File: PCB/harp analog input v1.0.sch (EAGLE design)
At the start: 109 parts, among them IC1 USBLC6-2SC6, IC10 SN74LVC1G125, IC11 SN74LVC1G125, IC12 SN74LVC1G125, IC13 AD7606-4, IC14 M74VHC1GT50DTT1G, IC15 M74VHC1GT50DTT1G, IC2 DC-DC-SIP-5, IC3 FT232RL, IC4 TPS78630DCQ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

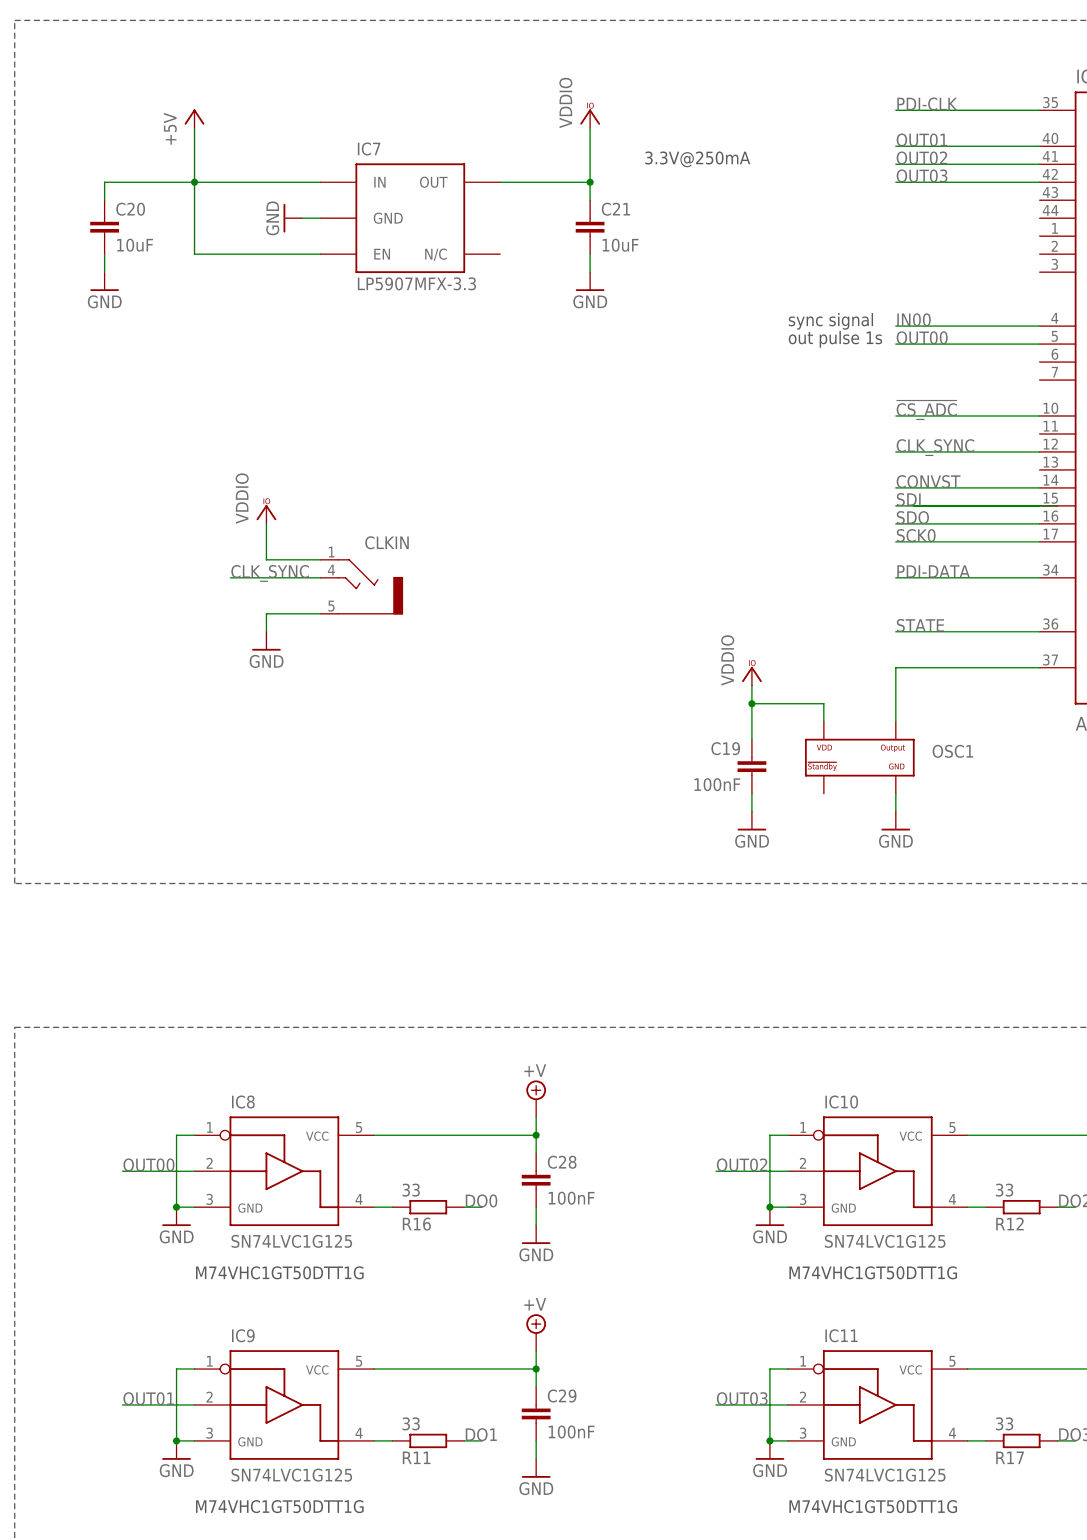
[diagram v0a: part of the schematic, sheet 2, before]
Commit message: Re-organized DO alignment from left (DO0) to right (DO3)
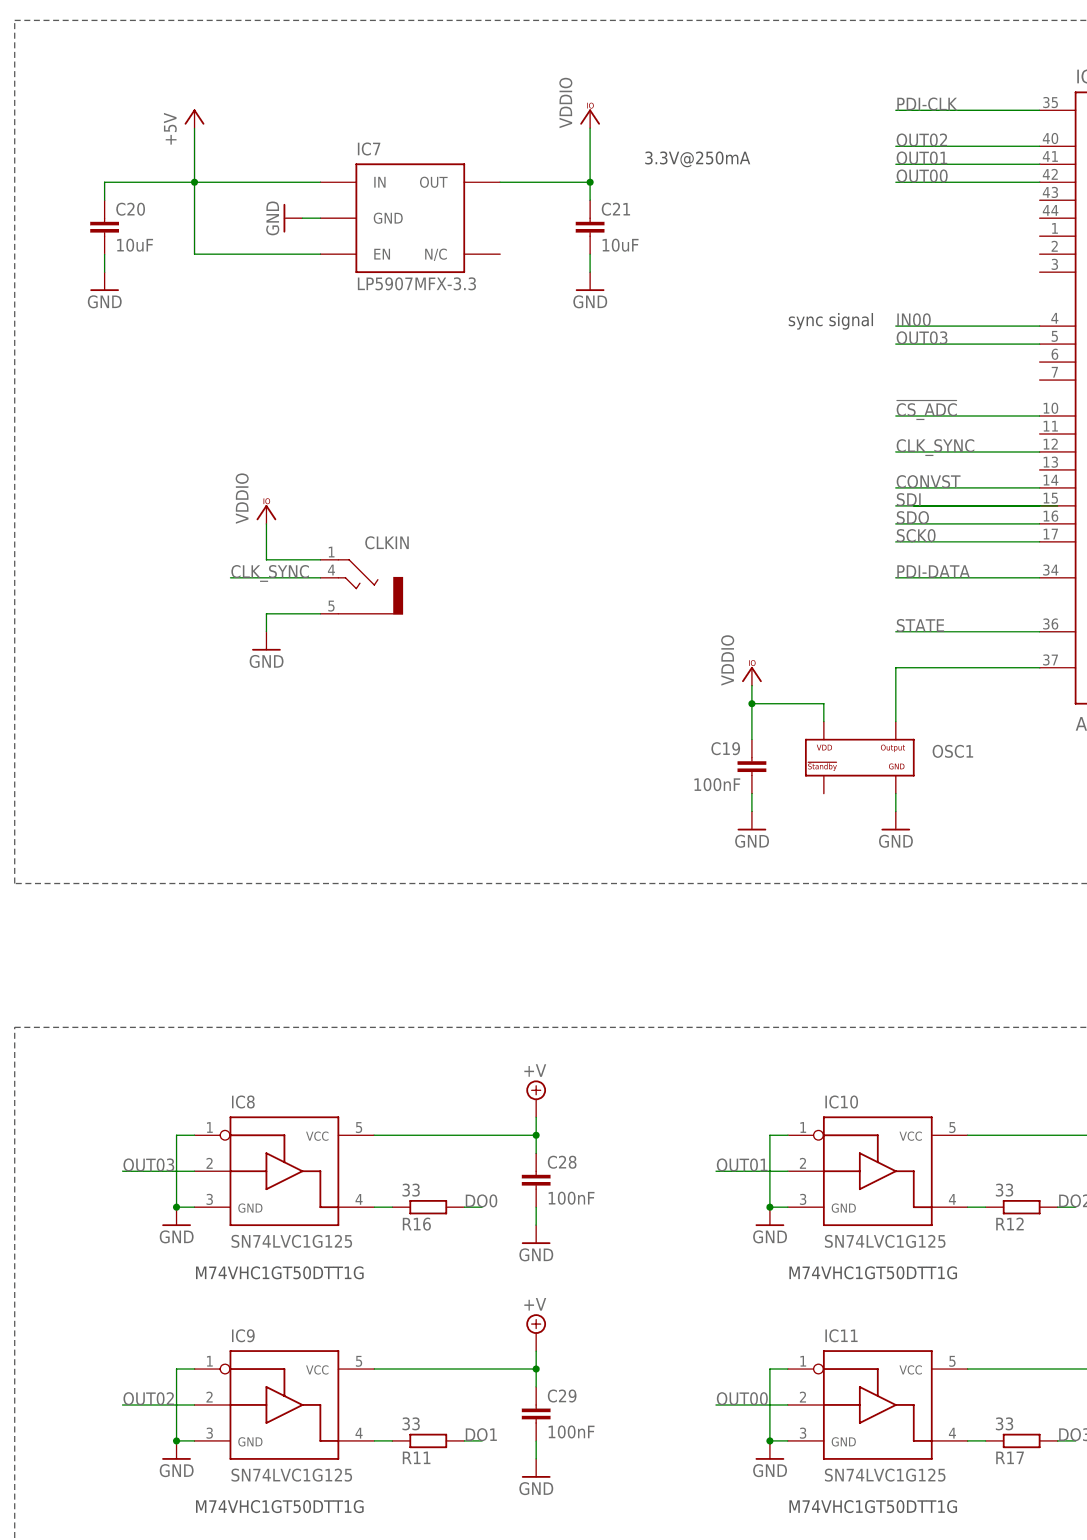
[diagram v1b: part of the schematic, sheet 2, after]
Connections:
- net OUT00: now also IC11.P$2, IC6.PA2/ADC2; no longer IC6.PB1/ADC9, IC8.P$2
- net OUT01: now also IC10.P$2, IC6.PA1/ADC1; no longer IC6.PA0/ADC0/AREF, IC9.P$2
- net OUT02: now also IC6.PA0/ADC0/AREF, IC9.P$2; no longer IC10.P$2, IC6.PA1/ADC1
- net OUT03: now also IC6.PB1/ADC9, IC8.P$2; no longer IC11.P$2, IC6.PA2/ADC2
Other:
- note removed: "out pulse 1s"
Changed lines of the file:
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@@
 <?xml version="1.0" encoding="utf-8"?>
 <!DOCTYPE eagle SYSTEM "eagle.dtd">
-<eagle version="9.6.2">
+<eagle version="9.5.1">
 <drawing>
 <settings>
@@
 <text x="109.22" y="226.06" size="1.778" layer="97">3.3V@250mA</text>
 <text x="129.54" y="203.2" size="1.778" layer="97">sync signal</text>
-<text x="129.54" y="200.66" size="1.778" layer="97">out pulse 1s</text>
 <text x="292.1" y="10.16" size="1.778" layer="94" ratio="10">Licensed under the TAPR Open
 Hardware License (www.tapr.org/OHL)
@@
 </segment>
 </net>
-<net name="OUT00" class="0">
+<net name="OUT03" class="0">
 <segment>
 <wire x1="165.1" y1="200.66" x2="144.78" y2="200.66" width="0.1524" layer="91"/>
@@
 </segment>
 </net>
-<net name="OUT03" class="0">
+<net name="OUT00" class="0">
 <segment>
 <wire x1="165.1" y1="223.52" x2="144.78" y2="223.52" width="0.1524" layer="91"/>
@@
 </segment>
 </net>
-<net name="OUT01" class="0">
+<net name="OUT02" class="0">
 <segment>
 <wire x1="165.1" y1="228.6" x2="144.78" y2="228.6" width="0.1524" layer="91"/>
@@
 </segment>
 </net>
-<net name="OUT02" class="0">
+<net name="OUT01" class="0">
 <segment>
 <wire x1="165.1" y1="226.06" x2="144.78" y2="226.06" width="0.1524" layer="91"/>

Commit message: Correct minor DRC and net labelling from merge
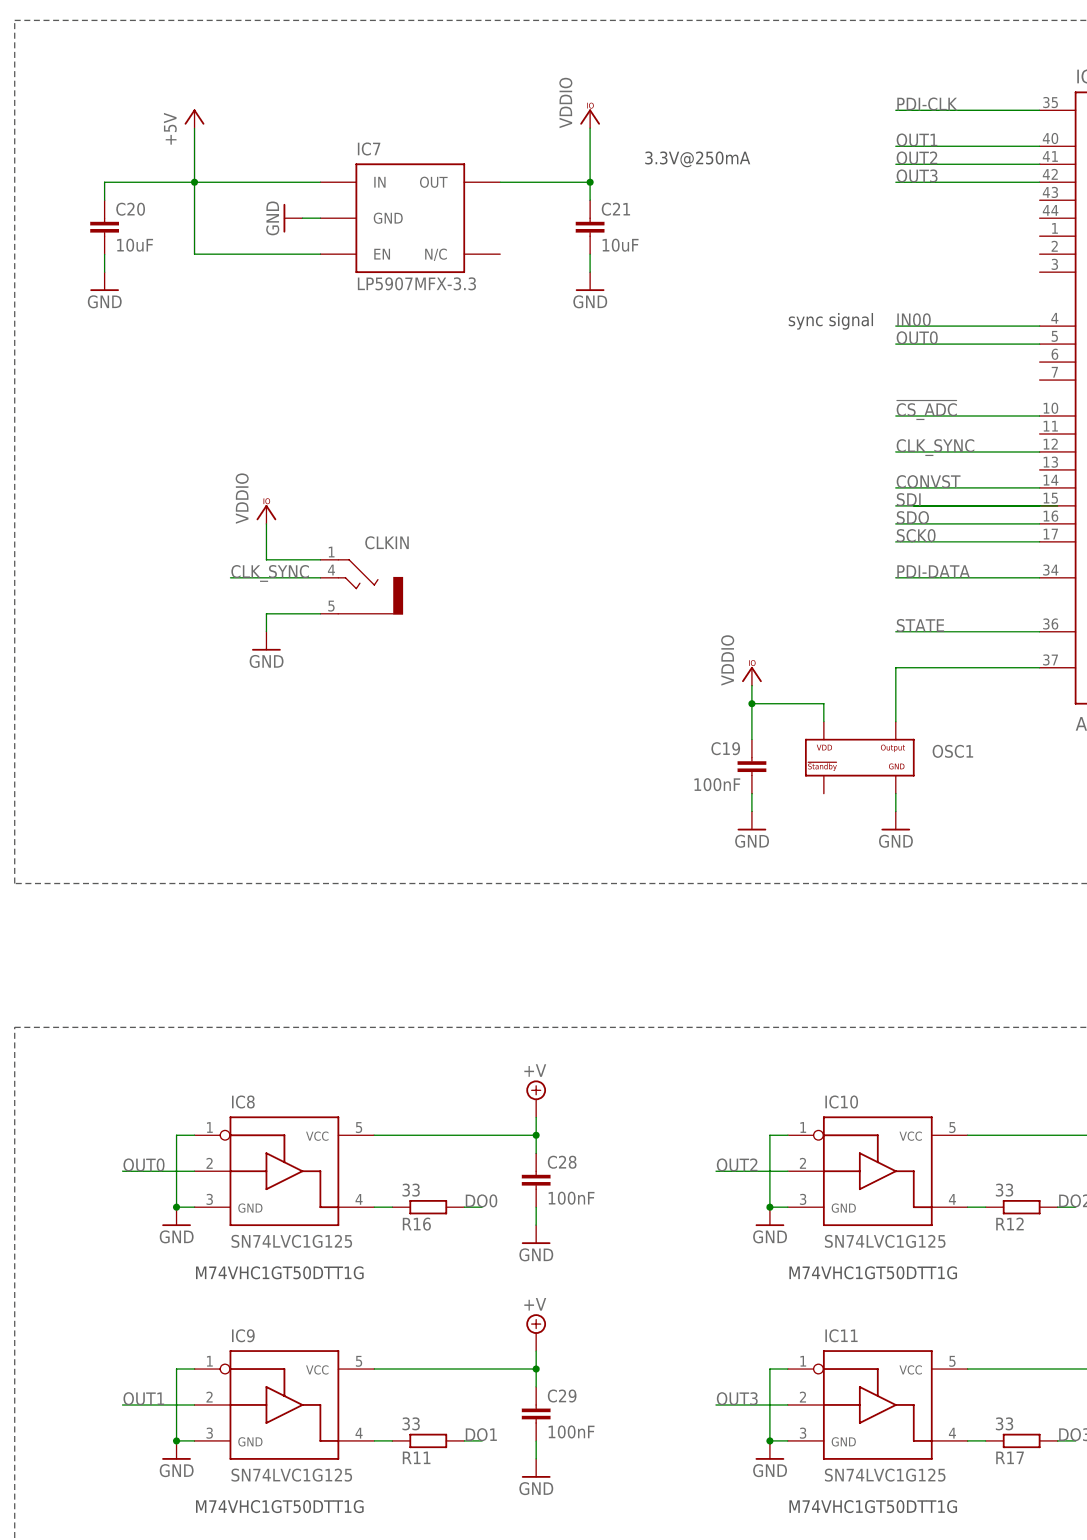
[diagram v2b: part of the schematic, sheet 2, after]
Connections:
- net OUT00 renamed OUT3
- net OUT01 renamed OUT2
- net OUT02 renamed OUT1
- net OUT03 renamed OUT0
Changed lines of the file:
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@@
 <?xml version="1.0" encoding="utf-8"?>
 <!DOCTYPE eagle SYSTEM "eagle.dtd">
-<eagle version="9.5.1">
+<eagle version="9.6.2">
 <drawing>
 <settings>
@@
 </segment>
 </net>
-<net name="OUT03" class="0">
+<net name="OUT0" class="0">
 <segment>
 <wire x1="165.1" y1="200.66" x2="144.78" y2="200.66" width="0.1524" layer="91"/>
@@
 </segment>
 </net>
-<net name="OUT00" class="0">
+<net name="OUT3" class="0">
 <segment>
 <wire x1="165.1" y1="223.52" x2="144.78" y2="223.52" width="0.1524" layer="91"/>
@@
 </segment>
 </net>
-<net name="OUT02" class="0">
+<net name="OUT1" class="0">
 <segment>
 <wire x1="165.1" y1="228.6" x2="144.78" y2="228.6" width="0.1524" layer="91"/>
@@
 </segment>
 </net>
-<net name="OUT01" class="0">
+<net name="OUT2" class="0">
 <segment>
 <wire x1="165.1" y1="226.06" x2="144.78" y2="226.06" width="0.1524" layer="91"/>

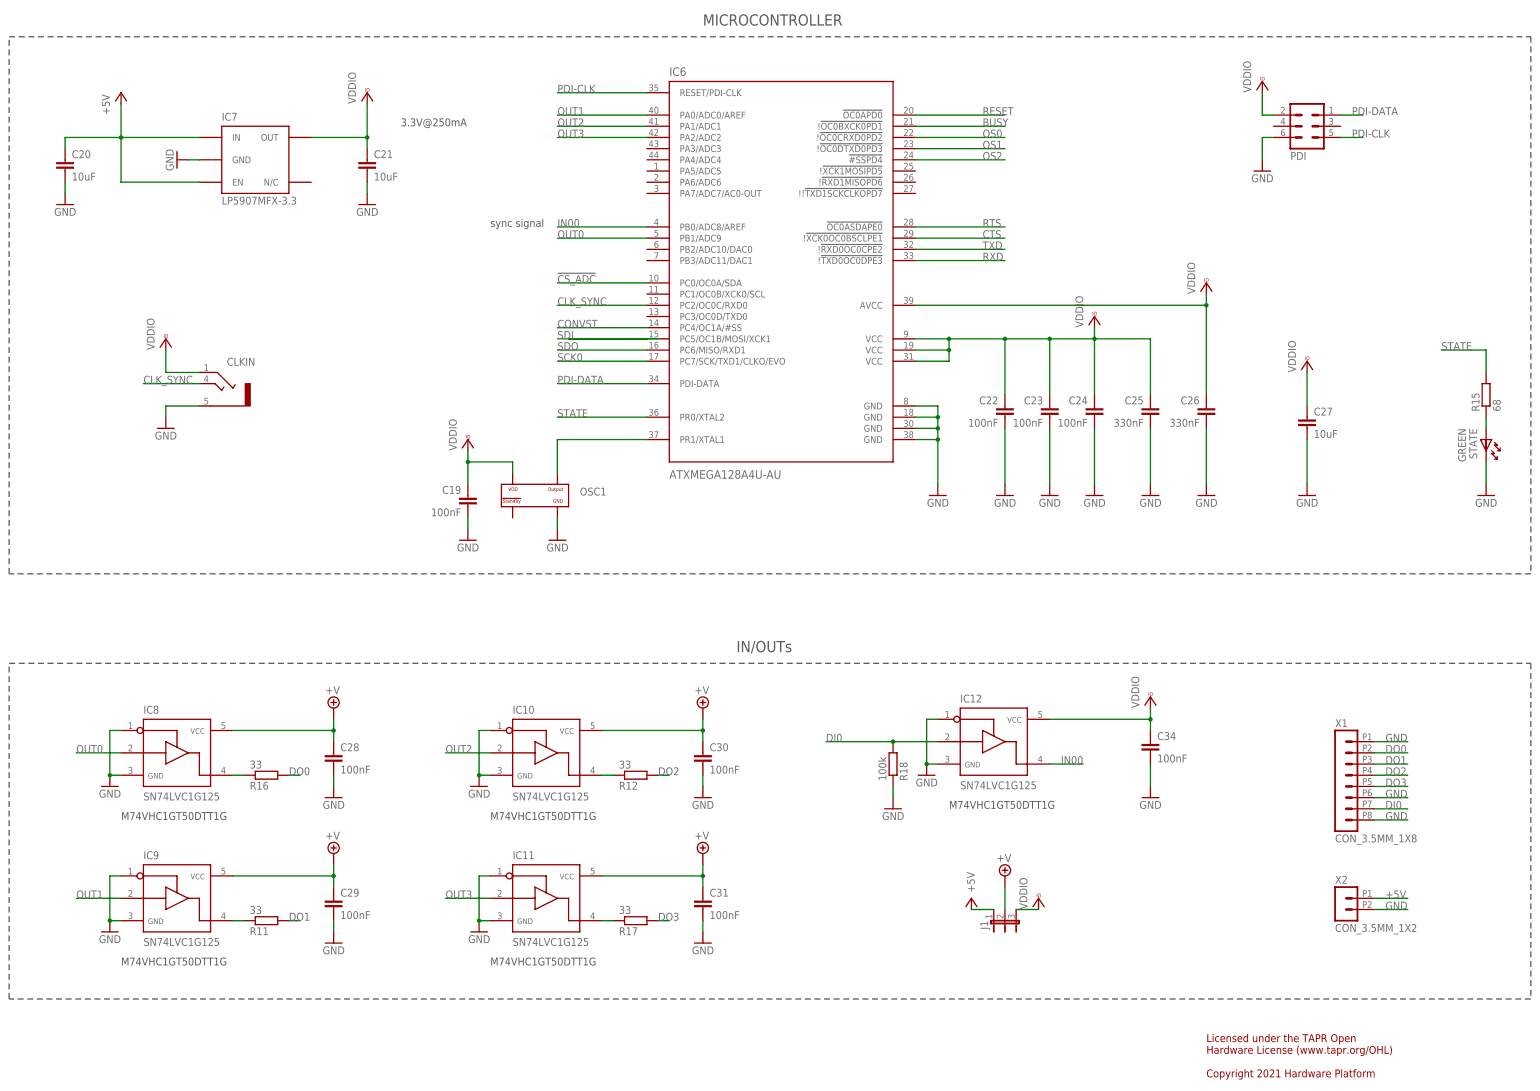
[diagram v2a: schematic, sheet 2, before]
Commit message: Add CONVST pin/swap CS_ADC
To allow for future higher speed acquisitions
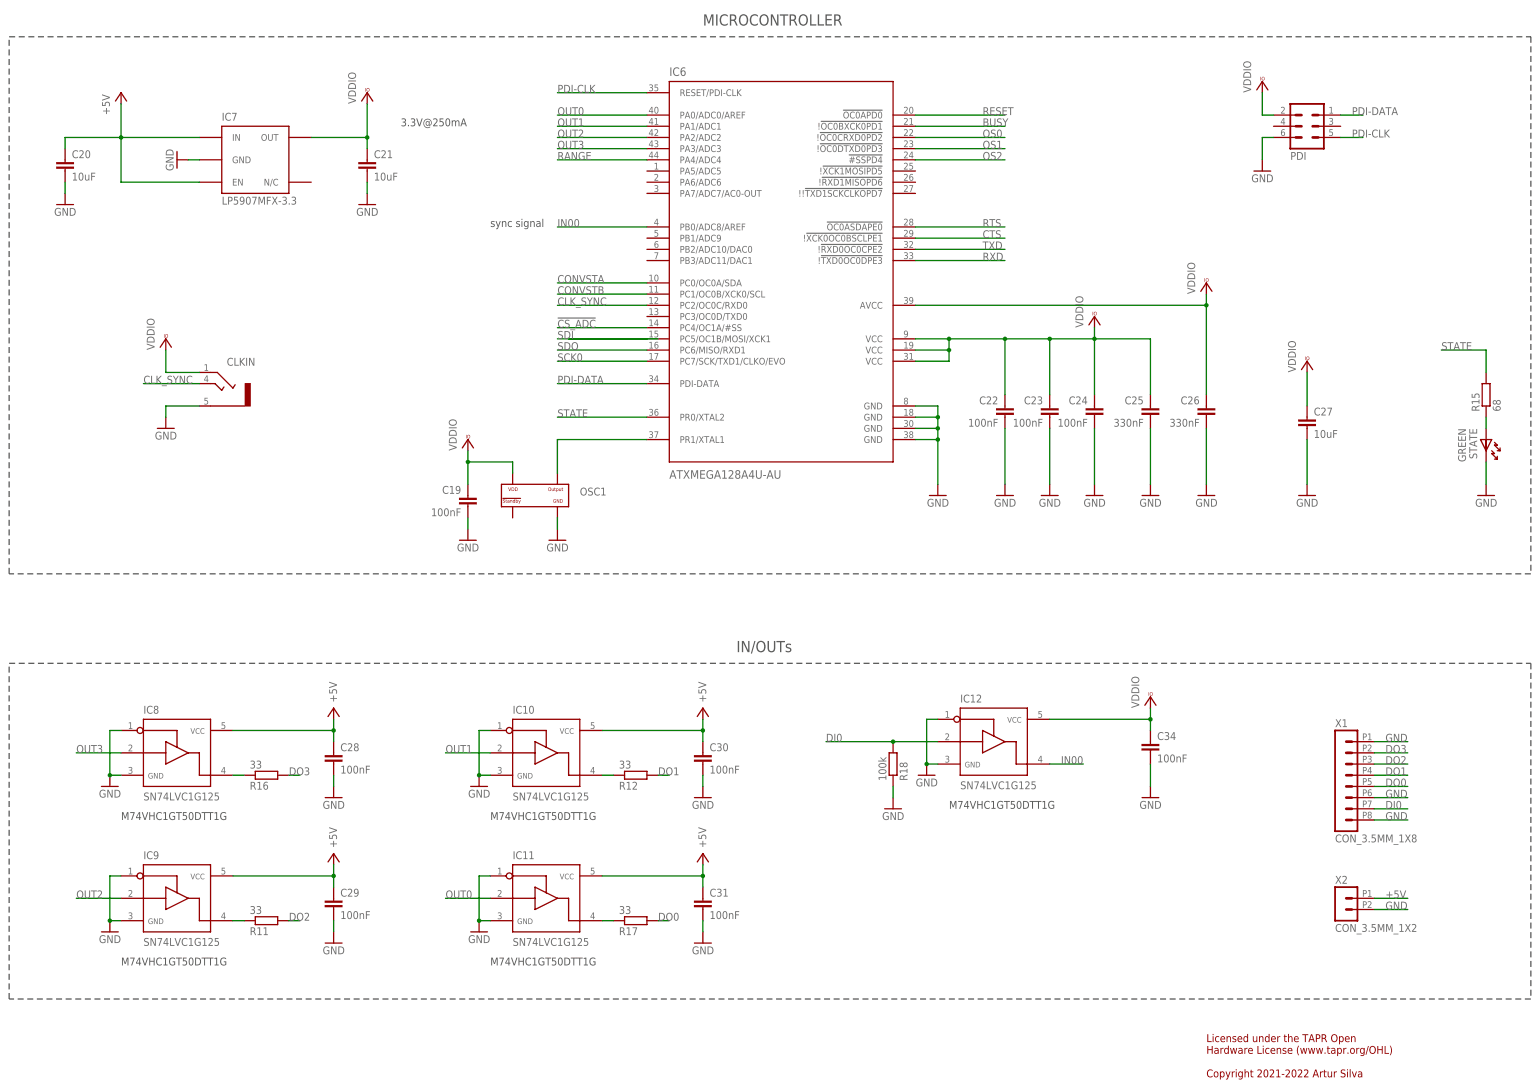
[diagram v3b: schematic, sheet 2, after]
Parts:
- removed CTUNE: NA, rcl:C-EUC0402
- removed J1: (no value), jumper:JP2E
- removed RTUNE: NA, rcl:R-EU_R0402
- C37: value 10uF -> 10uF NA
- C38, C40: value 100nF -> 100nF NA
- C39: value 1uF -> 1uF NA
- IC4: device CNP:TPS795XX -> CNP-ics 1:TPS78601SON
- R10, R21, R22, R24: value 100k -> NA
- R13: value 20k -> 20k NA
- R14: value 40.2k -> 40.2k NA
- R7: value 3k -> 3k NA
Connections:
- removed net +V: C28.1, C29.1, C30.1, C31.1, IC10.P$5, IC11.P$5, IC8.P$5, IC9.P$5, J1.2
- removed net CONVST: IC13.CONVSTA, IC13.CONVSTB, IC6.PC4/OC1A/#SS
- removed net N$1: IC13.RANGE, R10.1, R9.2
- removed net N$14: CTUNE.1, RTUNE.1
- new net CONVSTA: IC13.CONVSTA, IC6.PC0/OC0A/SDA
- new net CONVSTB: IC13.CONVSTB, IC6.PC1/OC0B/XCK0/SCL
- new net RANGE: IC13.RANGE, IC6.PA4/ADC4, R10.1, R9.2
- net !CS_ADC: now also IC6.PC4/OC1A/#SS; no longer IC6.PC0/OC0A/SDA
- net +5V: now also C28.1, C29.1, C30.1, C31.1, IC10.P$5, IC11.P$5, IC8.P$5, IC9.P$5; no longer J1.1
- net DO0: now also R17.2, X1.5; no longer R16.2, X1.2
- net DO1: now also R12.2, X1.4; no longer R11.2, X1.3
- net DO2: now also R11.2, X1.3; no longer R12.2, X1.4
- net DO3: now also R16.2, X1.2; no longer R17.2, X1.5
- net N$12: no longer CTUNE.2
- net OUT0: now also IC11.P$2, IC6.PA0/ADC0/AREF; no longer IC6.PB1/ADC9, IC8.P$2
- net OUT1: now also IC10.P$2, IC6.PA1/ADC1; no longer IC6.PA0/ADC0/AREF, IC9.P$2
- net OUT2: now also IC6.PA2/ADC2, IC9.P$2; no longer IC10.P$2, IC6.PA1/ADC1
- net OUT3: now also IC6.PA3/ADC3, IC8.P$2; no longer IC11.P$2, IC6.PA2/ADC2
- net P5.45V: no longer RTUNE.2
- net VCCIO: no longer J1.3
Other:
- note added: "Licensed under the TAPR Open Hardware License (www.tapr.org/OHL) Copyright 2021-2022 Artur Silva"
- note removed: "Licensed under the TAPR Open Hardware License (www.tapr.org/OHL) Copyright 2021 Hardware Platform"
